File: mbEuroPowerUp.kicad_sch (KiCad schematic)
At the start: 10 parts, among them J1 Conn_02x08_Odd_Even, J2 USB_B_Micro, J3 Conn_01x03, J4 Conn_02x02_Odd_Even, J5 Conn_01x02, J6 Conn_01x02

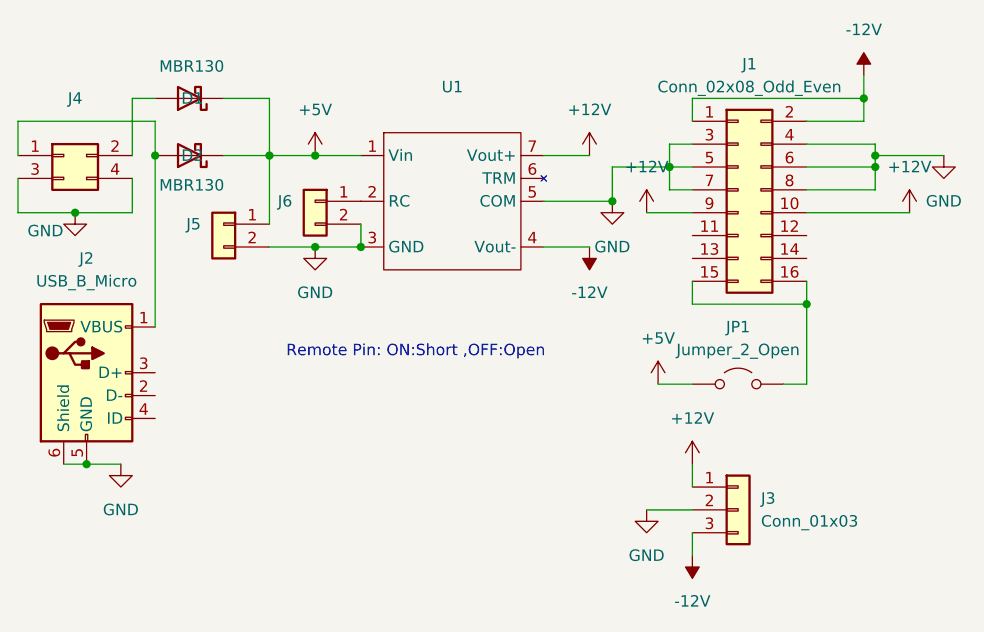
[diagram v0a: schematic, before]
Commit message: Fix 5V Pins
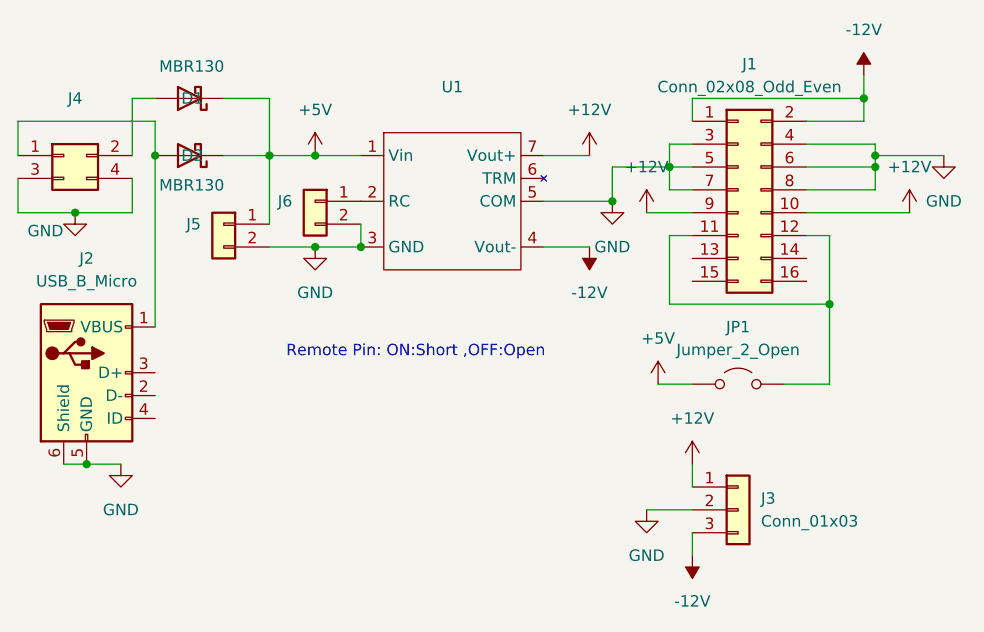
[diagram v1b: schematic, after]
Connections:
- net at J1.11 (Pin_11): now also J1.12 (Pin_12), JP1.2 (B)
- now unconnected: J1.15 (Pin_15), J1.16 (Pin_16)
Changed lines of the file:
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@@
+	)
+	(junction
+		(at 185.42 109.22)
+		(diameter 0)
+		(color 0 0 0 0)
 	)
 	(junction
@@
 	)
 	(junction
-		(at 182.88 109.22)
-		(diameter 0)
-		(color 0 0 0 0)
-	)
-	(junction
 		(at 167.64 93.98)
 		(diameter 0)
@@
 	(wire
 		(pts
-			(xy 170.18 109.22) (xy 182.88 109.22)
-		)
-		(stroke
-			(width 0)
-			(type default)
-		)
-	)
-	(wire
-		(pts
 			(xy 110.49 92.71) (xy 110.49 111.76)
 		)
@@
 	(wire
 		(pts
-			(xy 182.88 118.11) (xy 182.88 109.22)
+			(xy 185.42 118.11) (xy 185.42 109.22)
 		)
 		(stroke
@@
 	(wire
 		(pts
-			(xy 180.34 118.11) (xy 182.88 118.11)
+			(xy 167.64 101.6) (xy 170.18 101.6)
+		)
+		(stroke
+			(width 0)
+			(type default)
+		)
+	)
+	(wire
+		(pts
+			(xy 180.34 118.11) (xy 185.42 118.11)
 		)
 		(stroke
@@
 	(wire
 		(pts
-			(xy 182.88 106.68) (xy 182.88 109.22)
-		)
-		(stroke
-			(width 0)
-			(type default)
-		)
-	)
-	(wire
-		(pts
 			(xy 190.5 92.71) (xy 190.5 91.44)
 		)
@@
 	(wire
 		(pts
+			(xy 185.42 109.22) (xy 185.42 101.6)
+		)
+		(stroke
+			(width 0)
+			(type default)
+		)
+	)
+	(wire
+		(pts
 			(xy 190.5 92.71) (xy 198.12 92.71)
 		)
@@
 	(wire
 		(pts
+			(xy 185.42 101.6) (xy 182.88 101.6)
+		)
+		(stroke
+			(width 0)
+			(type default)
+		)
+	)
+	(wire
+		(pts
 			(xy 110.49 88.9) (xy 110.49 92.71)
 		)
@@
 	(wire
 		(pts
-			(xy 170.18 106.68) (xy 170.18 109.22)
-		)
-		(stroke
-			(width 0)
-			(type default)
-		)
-	)
-	(wire
-		(pts
 			(xy 107.95 95.25) (xy 107.95 99.06)
 		)
@@
 	(wire
 		(pts
+			(xy 167.64 109.22) (xy 167.64 101.6)
+		)
+		(stroke
+			(width 0)
+			(type default)
+		)
+	)
+	(wire
+		(pts
 			(xy 182.88 91.44) (xy 190.5 91.44)
 		)
 		(stroke
+			(width 0)
+			(type default)
+		)
+	)
+	(wire
+		(pts
+			(xy 167.64 109.22) (xy 185.42 109.22)
+		)
+		(stroke
